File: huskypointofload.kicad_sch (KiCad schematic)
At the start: 37 parts, among them J1 POWER, J2 VSENSE, J3 RFSOC_POWER, U1 INA290A2xDCK, U2 INA290A2xDCK

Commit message: Fix typo add bom
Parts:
- R5: value 49.9 -> 49.9k
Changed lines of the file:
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@@
 			)
 		)
-		(property "Value" "49.9"
+		(property "Value" "49.9k"
 			(at 181.61 121.9199 0)
 			(effects

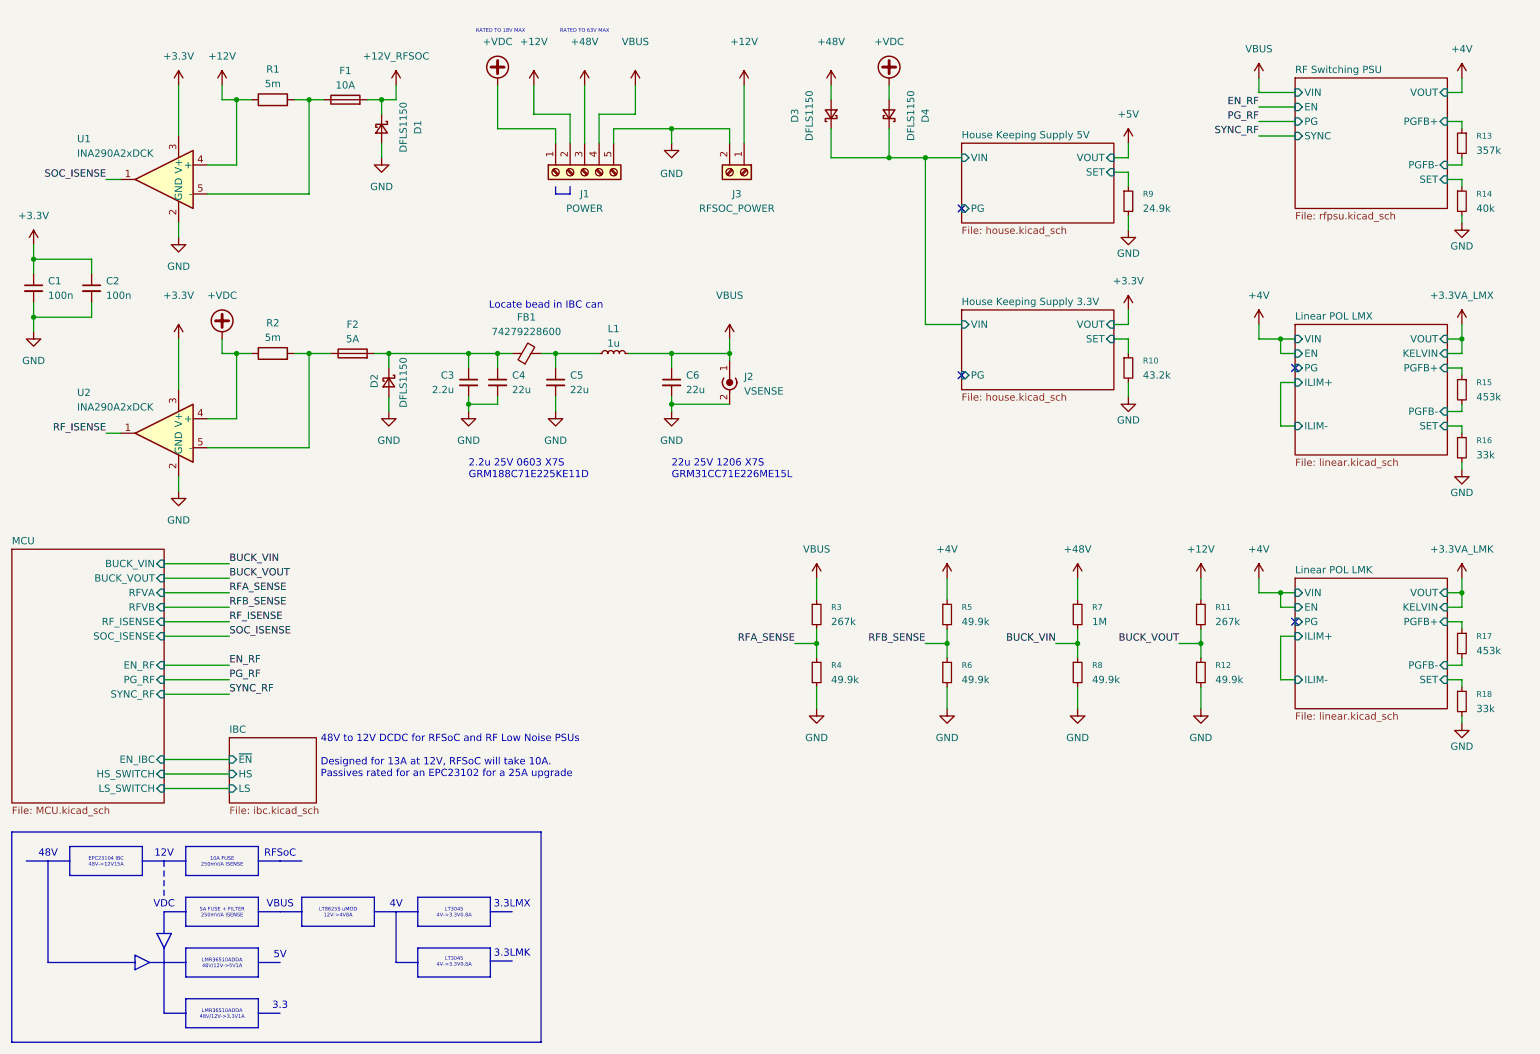
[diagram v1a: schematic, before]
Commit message: reorg and add 10MHz
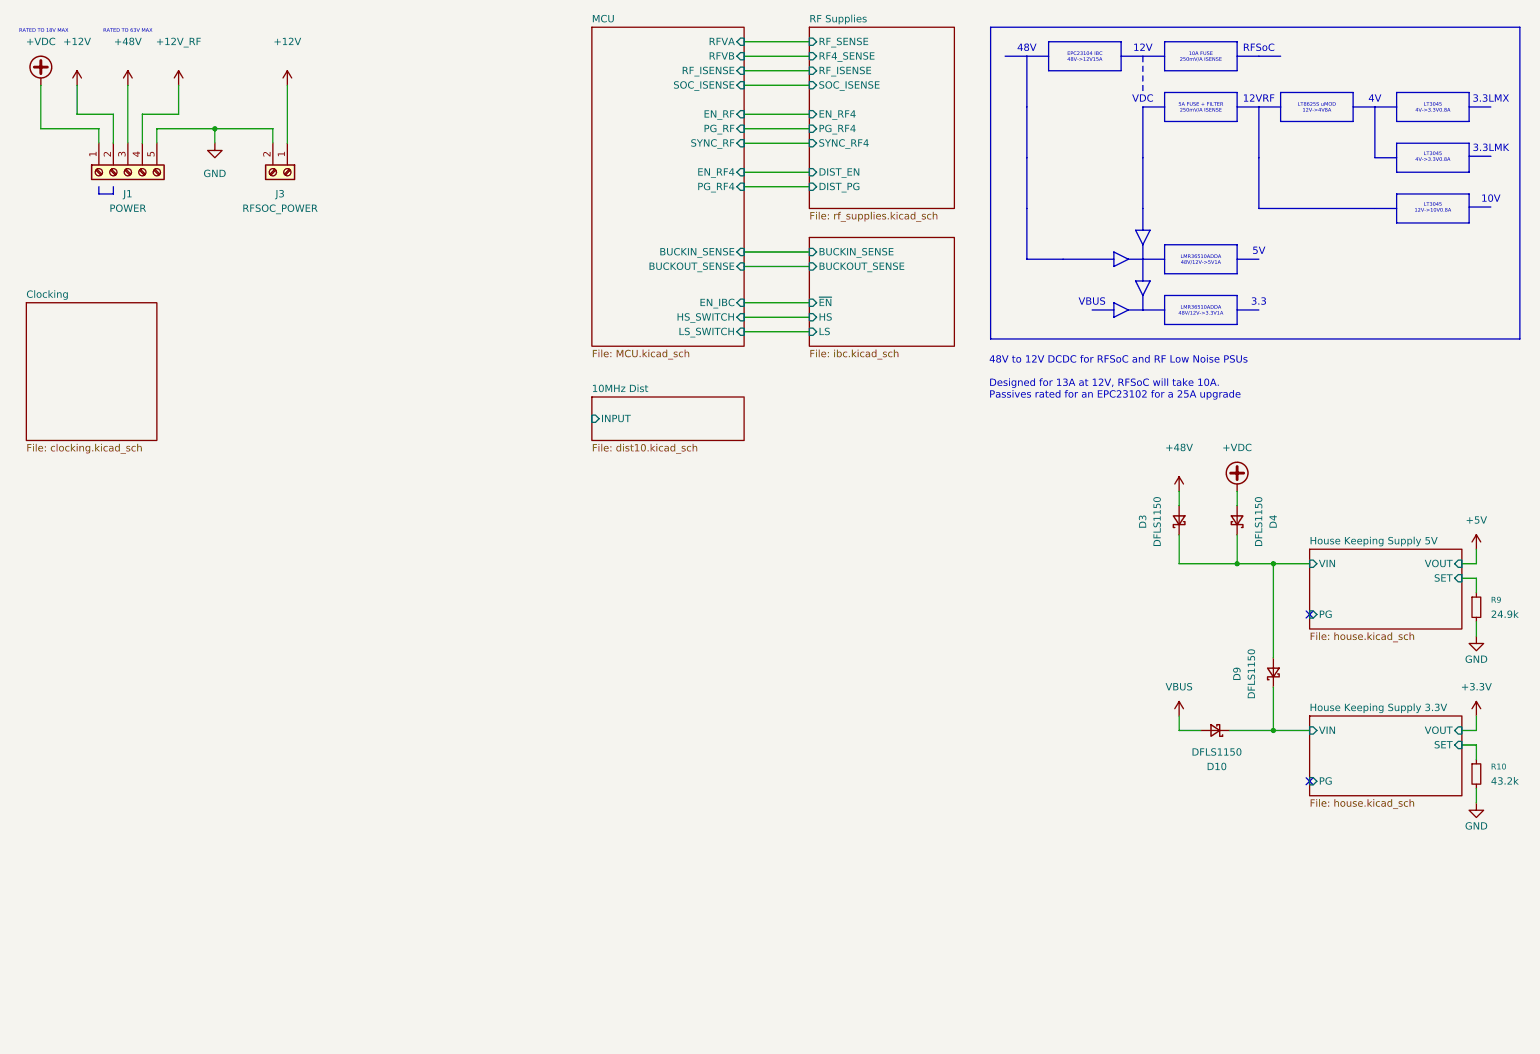
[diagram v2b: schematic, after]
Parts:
- removed C1, C2: 100n, Capacitor_SMD:C_0402_1005Metric, symbol Device:C_Small
- removed C3: 2.2u, Capacitor_SMD:C_0603_1608Metric, symbol Device:C_Small
- removed C4, C5, C6: 22u, Capacitor_SMD:C_1206_3216Metric, symbol Device:C_Small
- removed D1, D2: DFLS1150, Diode_SMD:D_PowerDI-123, symbol Device:D_Schottky_Small
- removed F1: 10A, Fuse:Fuseholder_Littelfuse_Nano2_157x, symbol Device:Fuse
- removed F2: 5A, Fuse:Fuseholder_Littelfuse_Nano2_157x, symbol Device:Fuse
- removed FB1: 74279228600, Inductor_SMD:L_0603_1608Metric, symbol Device:FerriteBead_Small
- removed J2: VSENSE, Connector_Coaxial:SMA_Amphenol_132134-10_Vertical, symbol Connector:Conn_Coaxial_Power
- removed L1: 1u, Inductor_SMD:L_Bourns_SRR1260, symbol Device:L_Small
- removed R1, R2: 5m, Resistor_SMD:R_2512_6332Metric, symbol Device:R
- removed R11, R3: 267k, Resistor_SMD:R_0402_1005Metric, symbol Device:R_Small
- removed R12, R4, R5, R6, R8: 49.9k, Resistor_SMD:R_0402_1005Metric, symbol Device:R_Small
- removed R13: 357k, Resistor_SMD:R_0402_1005Metric, symbol Device:R_Small
- removed R14: 40k, Resistor_SMD:R_0402_1005Metric, symbol Device:R_Small
- removed R15, R17: 453k, Resistor_SMD:R_0402_1005Metric, symbol Device:R_Small
- removed R16, R18: 33k, Resistor_SMD:R_0402_1005Metric, symbol Device:R_Small
- removed R7: 1M, Resistor_SMD:R_0402_1005Metric, symbol Device:R_Small
- removed U1, U2: INA290A2xDCK, Package_TO_SOT_SMD:SOT-353_SC-70-5, symbol Amplifier_Current:INA290A2xDCK
- added D10, D9: DFLS1150, Diode_SMD:D_PowerDI-123, symbol Device:D_Schottky_Small
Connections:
- net House Keeping Supply 3.3V/VIN: now also D10.1 (K), D9.1 (K); no longer D3.1 (K), D4.1 (K)
- net VBUS: now also D10.2 (A); no longer J1.4 (Pin_4)
- new net +12V_RF: J1.4 (Pin_4)
- new net House Keeping Supply 5V/VIN: D3.1 (K), D4.1 (K), D9.2 (A)
- no-connect marks 4 -> 2
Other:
- removed sheet Linear POL LMK
- removed sheet Linear POL LMX
- removed sheet RF Switching PSU
- added sheet 10MHz Dist (dist10.kicad_sch)
- added sheet Clocking (clocking.kicad_sch)
- added sheet RF Supplies (rf_supplies.kicad_sch)
- sheet IBC ports: added BUCKIN_SENSE, BUCKOUT_SENSE; removed none
- sheet MCU ports: added BUCKIN_SENSE, BUCKOUT_SENSE, EN_RF4, PG_RF4; removed BUCK_VIN, BUCK_VOUT
- note added: "10V"
- note added: "12VRF"
- note added: "LT3045 12V->10V0.8A"
- note removed: "2.2u 25V 0603 X7S GRM188C71E225KE11D"
- note removed: "22u 25V 1206 X7S GRM31CC71E226ME15L"
- note removed: "Locate bead in IBC can"
- moved on the sheet: D3, D4, J1, J3, R10, R9

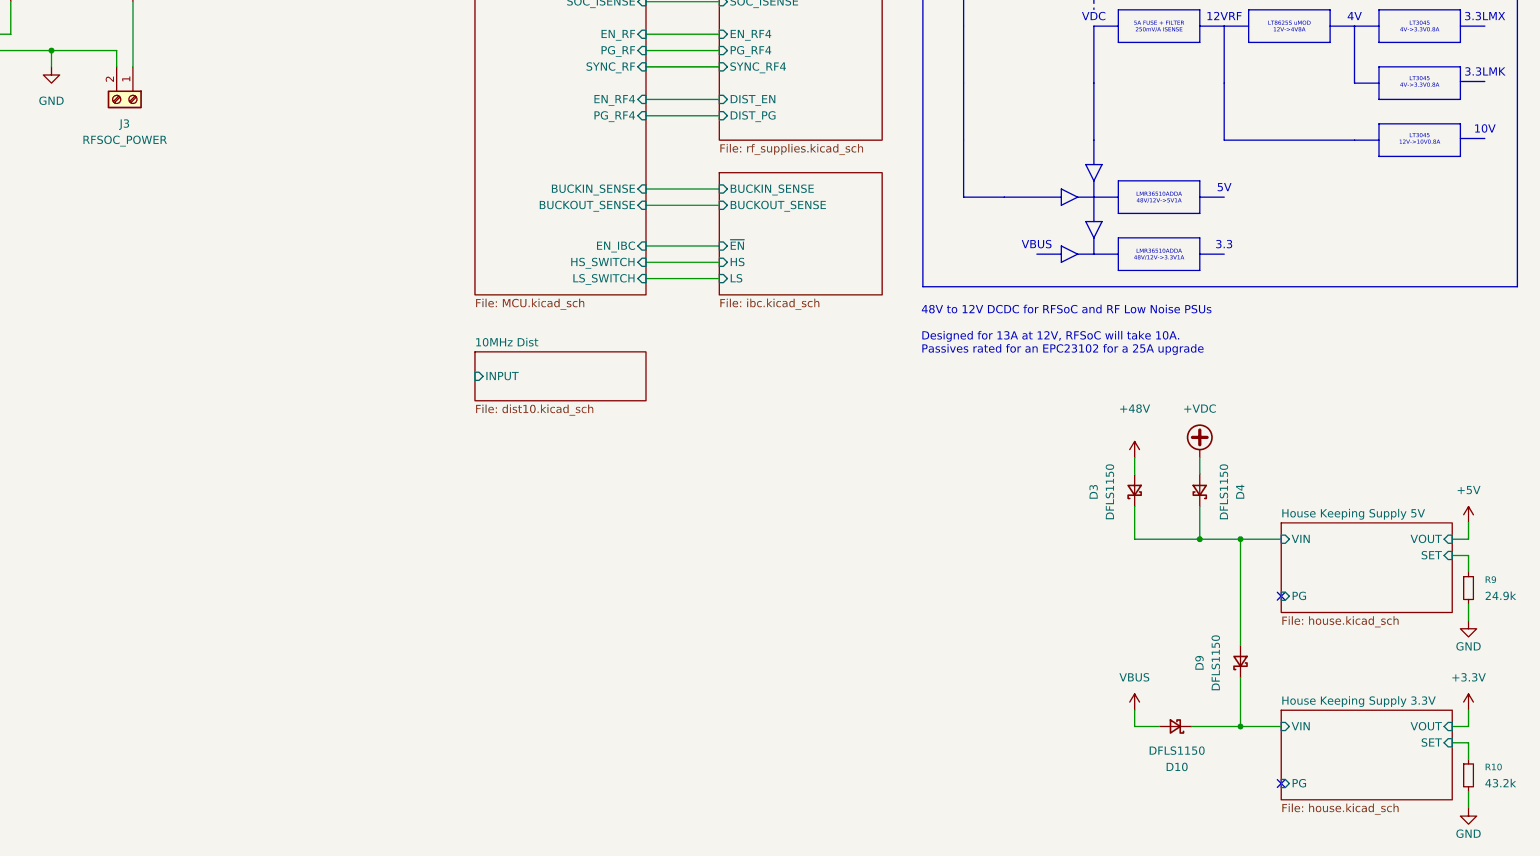
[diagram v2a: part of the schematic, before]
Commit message: Renumber refdes
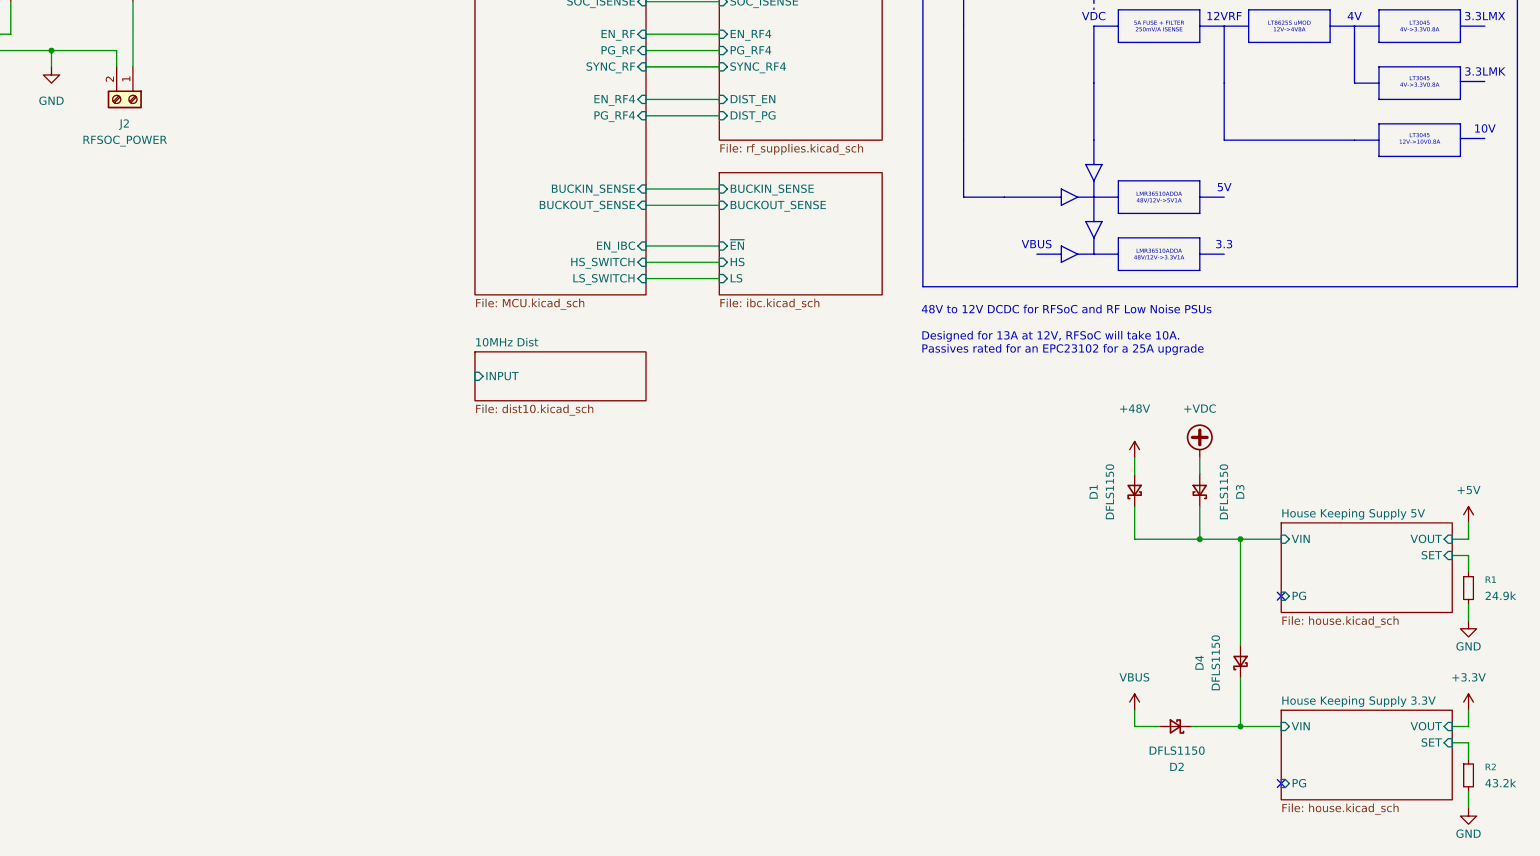
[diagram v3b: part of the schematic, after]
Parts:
- renumbered D3 to D1, D10 to D2, D4 to D3, D9 to D4, J3 to J2, R9 to R1, R10 to R2
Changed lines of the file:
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@@
 		(dnp no)
 		(fields_autoplaced yes)
-		(property "Reference" "#PWR025"
+		(property "Reference" "#PWR09"
 			(at 229.87 101.6 0)
 			(effects
@@
 			(project "huskypointofload"
 				(path "/eb9c972b-d134-41da-be97-ece3f463f7e0"
-					(reference "#PWR025")
+					(reference "#PWR09")
 					(unit 1)
 				)
@@
 		(on_board yes)
 		(dnp no)
-		(property "Reference" "#PWR016"
+		(property "Reference" "#PWR03"
 			(at 35.56 31.75 0)
 			(effects
@@
 			(project ""
 				(path "/eb9c972b-d134-41da-be97-ece3f463f7e0"
-					(reference "#PWR016")
+					(reference "#PWR03")
 					(unit 1)
 				)
@@
 		(on_board yes)
 		(dnp no)
-		(property "Reference" "D4"
+		(property "Reference" "D3"
 			(at 236.22 104.394 0)
 			(effects
@@
 			(project "huskypointofload"
 				(path "/eb9c972b-d134-41da-be97-ece3f463f7e0"
-					(reference "D4")
+					(reference "D3")
 					(unit 1)
 				)
@@
 		(dnp no)
 		(fields_autoplaced yes)
-		(property "Reference" "#PWR013"
+		(property "Reference" "#PWR01"
 			(at 20.32 30.48 0)
 			(effects
@@
 			(project "huskypointofload"
 				(path "/eb9c972b-d134-41da-be97-ece3f463f7e0"
-					(reference "#PWR013")
+					(reference "#PWR01")
 					(unit 1)
 				)
@@
 		(on_board yes)
 		(dnp no)
-		(property "Reference" "#PWR017"
+		(property "Reference" "#PWR04"
 			(at 44.45 31.75 0)
 			(effects
@@
 			(project "huskypointofload"
 				(path "/eb9c972b-d134-41da-be97-ece3f463f7e0"
-					(reference "#PWR017")
+					(reference "#PWR04")
 					(unit 1)
 				)
@@
 		(on_board yes)
 		(dnp no)
-		(property "Reference" "#PWR031"
+		(property "Reference" "#PWR011"
 			(at 271.78 130.81 0)
 			(effects
@@
 			(project ""
 				(path "/eb9c972b-d134-41da-be97-ece3f463f7e0"
-					(reference "#PWR031")
+					(reference "#PWR011")
 					(unit 1)
 				)
@@
 		(dnp no)
 		(fields_autoplaced yes)
-		(property "Reference" "R9"
+		(property "Reference" "R1"
 			(at 274.32 118.1099 0)
 			(effects
@@
 			(project ""
 				(path "/eb9c972b-d134-41da-be97-ece3f463f7e0"
-					(reference "R9")
+					(reference "R1")
 					(unit 1)
 				)
@@
 		(dnp no)
 		(fields_autoplaced yes)
-		(property "Reference" "R10"
+		(property "Reference" "R2"
 			(at 274.32 147.3199 0)
 			(effects
@@
 			(project "huskypointofload"
 				(path "/eb9c972b-d134-41da-be97-ece3f463f7e0"
-					(reference "R10")
+					(reference "R2")
 					(unit 1)
 				)
@@
 		(on_board yes)
 		(dnp no)
-		(property "Reference" "D10"
+		(property "Reference" "D2"
 			(at 226.314 147.32 0)
 			(effects
@@
 			(project "huskypointofload"
 				(path "/eb9c972b-d134-41da-be97-ece3f463f7e0"
-					(reference "D10")
+					(reference "D2")
 					(unit 1)
 				)
@@
 		(dnp no)
 		(fields_autoplaced yes)
-		(property "Reference" "#PWR032"
+		(property "Reference" "#PWR012"
 			(at 271.78 142.24 0)
 			(effects
@@
 			(project ""
 				(path "/eb9c972b-d134-41da-be97-ece3f463f7e0"
-					(reference "#PWR032")
+					(reference "#PWR012")
 					(unit 1)
 				)
@@
 		(on_board yes)
 		(dnp no)
-		(property "Reference" "#PWR024"
+		(property "Reference" "#PWR07"
 			(at 219.71 102.87 0)
 			(effects
@@
 			(project "huskypointofload"
 				(path "/eb9c972b-d134-41da-be97-ece3f463f7e0"
-					(reference "#PWR024")
+					(reference "#PWR07")
 					(unit 1)
 				)
@@
 		(on_board yes)
 		(dnp no)
-		(property "Reference" "D3"
+		(property "Reference" "D1"
 			(at 213.36 104.394 0)
 			(effects
@@
 			(project "huskypointofload"
 				(path "/eb9c972b-d134-41da-be97-ece3f463f7e0"
-					(reference "D3")
+					(reference "D1")
 					(unit 1)
 				)
@@
 		(on_board yes)
 		(dnp no)
-		(property "Reference" "#PWR033"
+		(property "Reference" "#PWR013"
 			(at 271.78 160.02 0)
 			(effects
@@
 			(project "huskypointofload"
 				(path "/eb9c972b-d134-41da-be97-ece3f463f7e0"
-					(reference "#PWR033")
+					(reference "#PWR013")
 					(unit 1)
 				)
@@
 		(on_board yes)
 		(dnp no)
-		(property "Reference" "J3"
+		(property "Reference" "J2"
 			(at 62.23 46.99 90)
 			(effects
@@
 			(project ""
 				(path "/eb9c972b-d134-41da-be97-ece3f463f7e0"
-					(reference "J3")
+					(reference "J2")
 					(unit 1)
 				)
@@
 		(dnp no)
 		(fields_autoplaced yes)
-		(property "Reference" "#PWR073"
+		(property "Reference" "#PWR08"
 			(at 219.71 142.24 0)
 			(effects
@@
 			(project "huskypointofload"
 				(path "/eb9c972b-d134-41da-be97-ece3f463f7e0"
-					(reference "#PWR073")
+					(reference "#PWR08")
 					(unit 1)
 				)
@@
 		(on_board yes)
 		(dnp no)
-		(property "Reference" "#PWR014"
+		(property "Reference" "#PWR02"
 			(at 26.67 31.75 0)
 			(effects
@@
 			(project ""
 				(path "/eb9c972b-d134-41da-be97-ece3f463f7e0"
-					(reference "#PWR014")
+					(reference "#PWR02")
 					(unit 1)
 				)
@@
 		(on_board yes)
 		(dnp no)
-		(property "Reference" "#PWR018"
+		(property "Reference" "#PWR05"
 			(at 50.8 44.45 0)
 			(effects
@@
 			(project ""
 				(path "/eb9c972b-d134-41da-be97-ece3f463f7e0"
-					(reference "#PWR018")
+					(reference "#PWR05")
 					(unit 1)
 				)
@@
 		(on_board yes)
 		(dnp no)
-		(property "Reference" "D9"
+		(property "Reference" "D4"
 			(at 229.87 131.064 0)
 			(effects
@@
 			(project "huskypointofload"
 				(path "/eb9c972b-d134-41da-be97-ece3f463f7e0"
-					(reference "D9")
+					(reference "D4")
 					(unit 1)
 				)
@@
 		(dnp no)
 		(fields_autoplaced yes)
-		(property "Reference" "#PWR030"
+		(property "Reference" "#PWR010"
 			(at 271.78 113.03 0)
 			(effects
@@
 			(project ""
 				(path "/eb9c972b-d134-41da-be97-ece3f463f7e0"
-					(reference "#PWR030")
+					(reference "#PWR010")
 					(unit 1)
 				)
@@
 		(on_board yes)
 		(dnp no)
-		(property "Reference" "#PWR021"
+		(property "Reference" "#PWR06"
 			(at 63.5 31.75 0)
 			(effects
@@
 			(project "huskypointofload"
 				(path "/eb9c972b-d134-41da-be97-ece3f463f7e0"
-					(reference "#PWR021")
-					(unit 1)
-				)
+					(reference "#PWR06")
+					(unit 1)
+				)
